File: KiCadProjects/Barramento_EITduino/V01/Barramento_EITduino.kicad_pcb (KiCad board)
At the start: 2 copper layers, 90 x 100 mm, 3 parts, among them J2 tensoes, J3 sinais analogicos, J4 comunicacao / sinais digitais

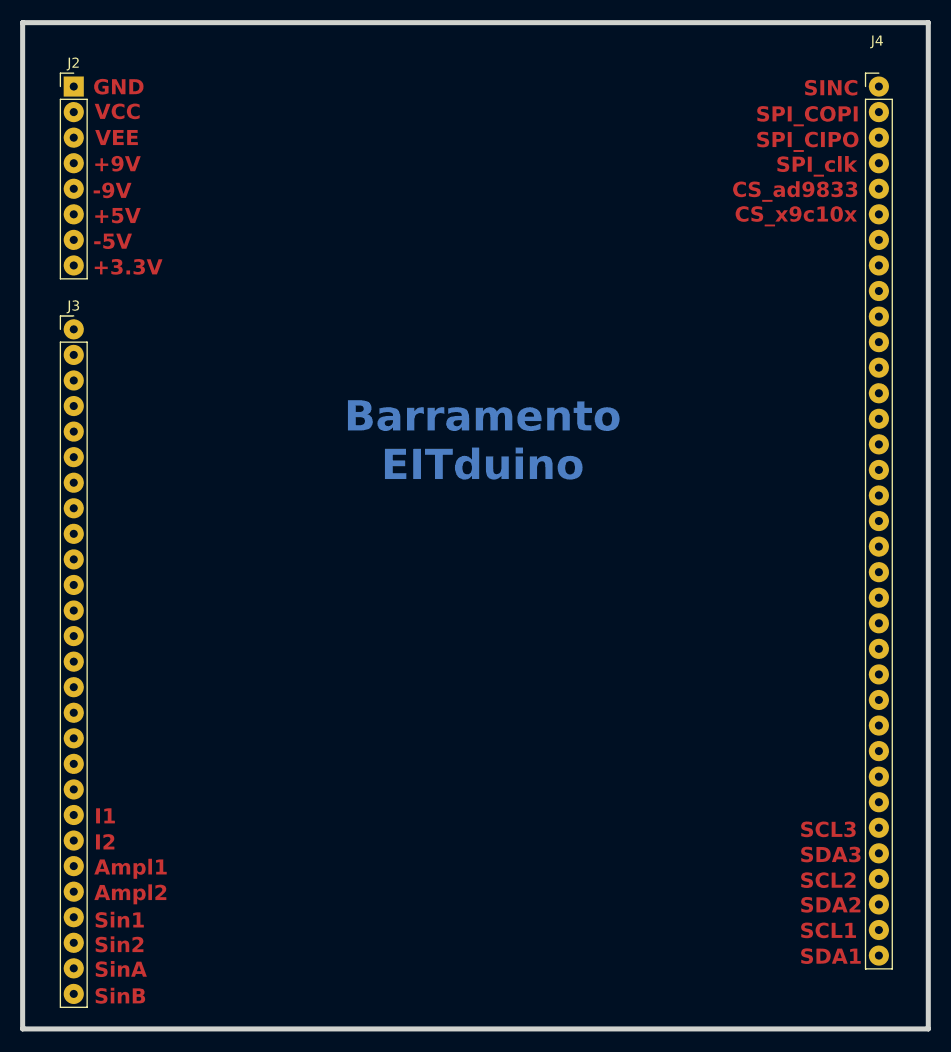
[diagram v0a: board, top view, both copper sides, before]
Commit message: Primeira versao de barramento - apenas um pino de terra
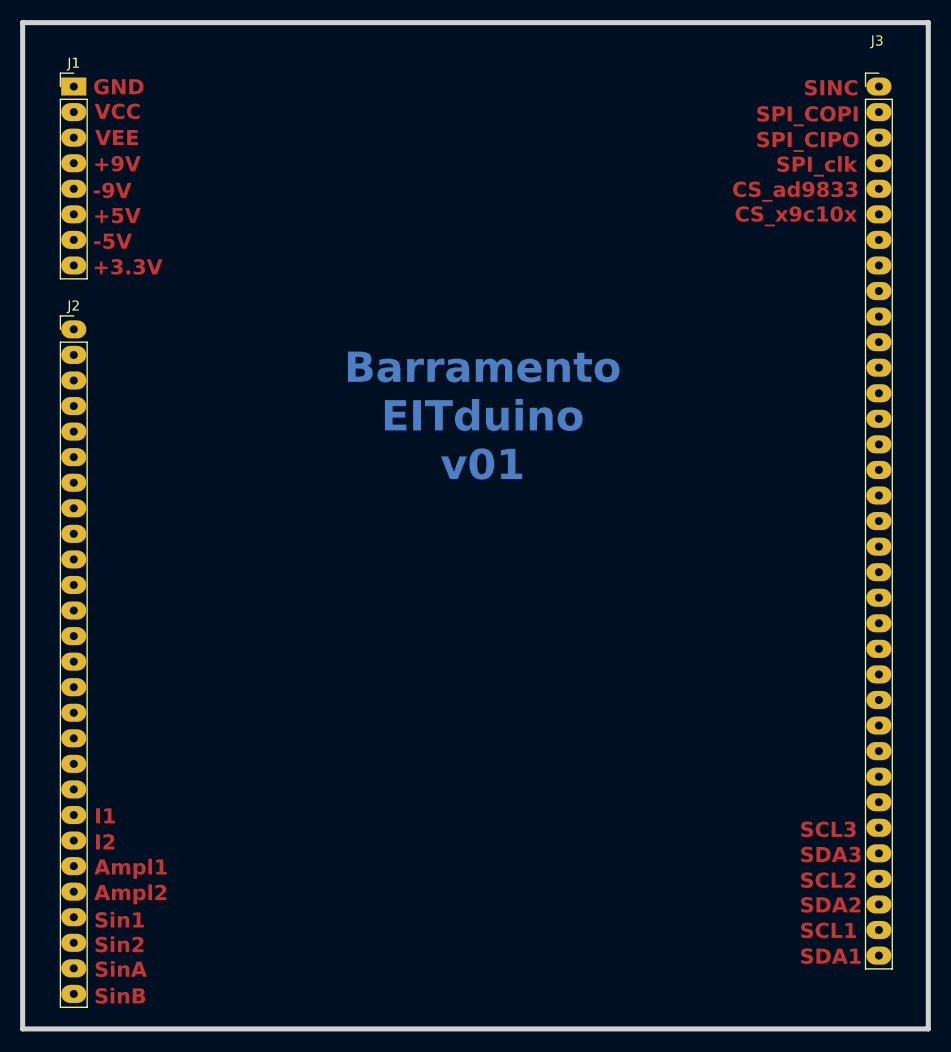
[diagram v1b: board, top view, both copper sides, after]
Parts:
- renumbered J2 to J1, J3 to J2, J4 to J3
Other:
- board text added: "Barramento EITduino v01"
- board text removed: "Barramento EITduino"
